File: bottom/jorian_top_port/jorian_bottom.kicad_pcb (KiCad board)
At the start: 2 copper layers, 152.4 x 85.1 mm, 7 parts

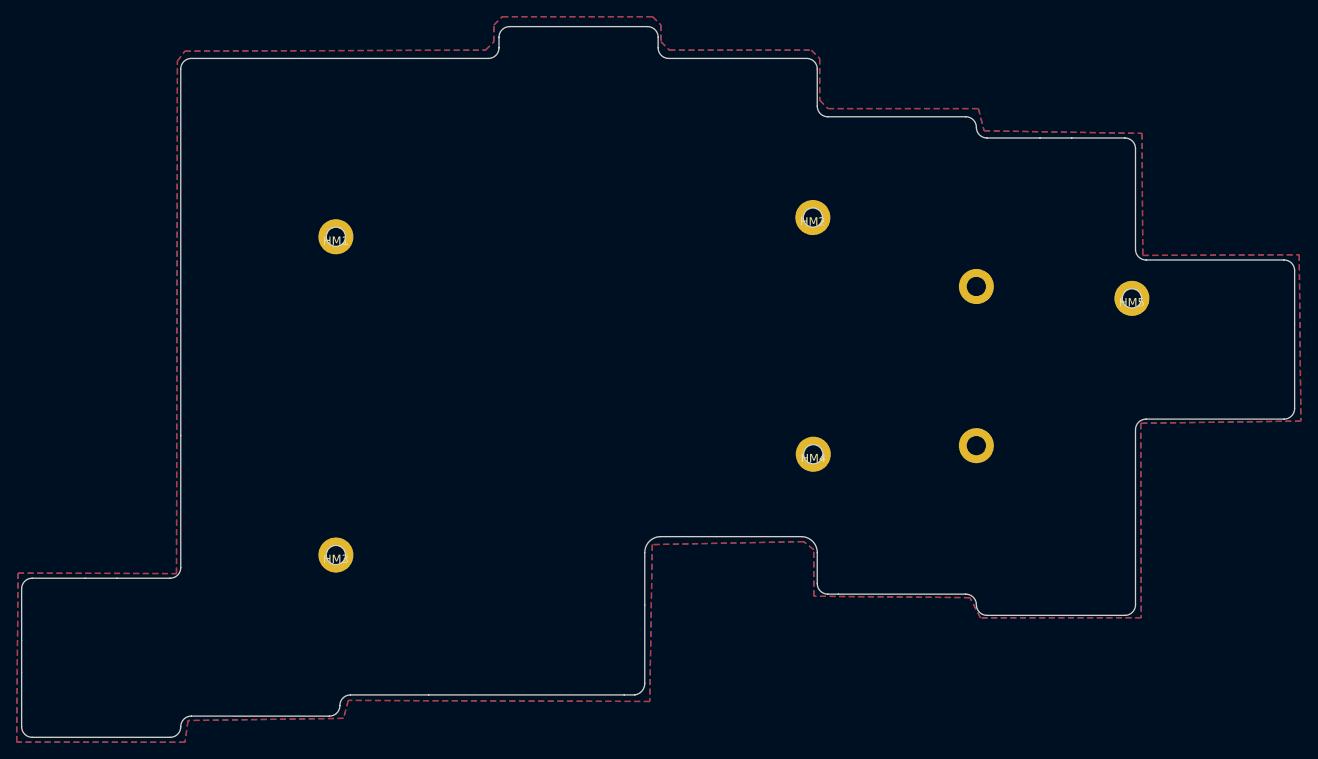
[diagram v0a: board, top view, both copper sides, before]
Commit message: Work on bottom with AA holder
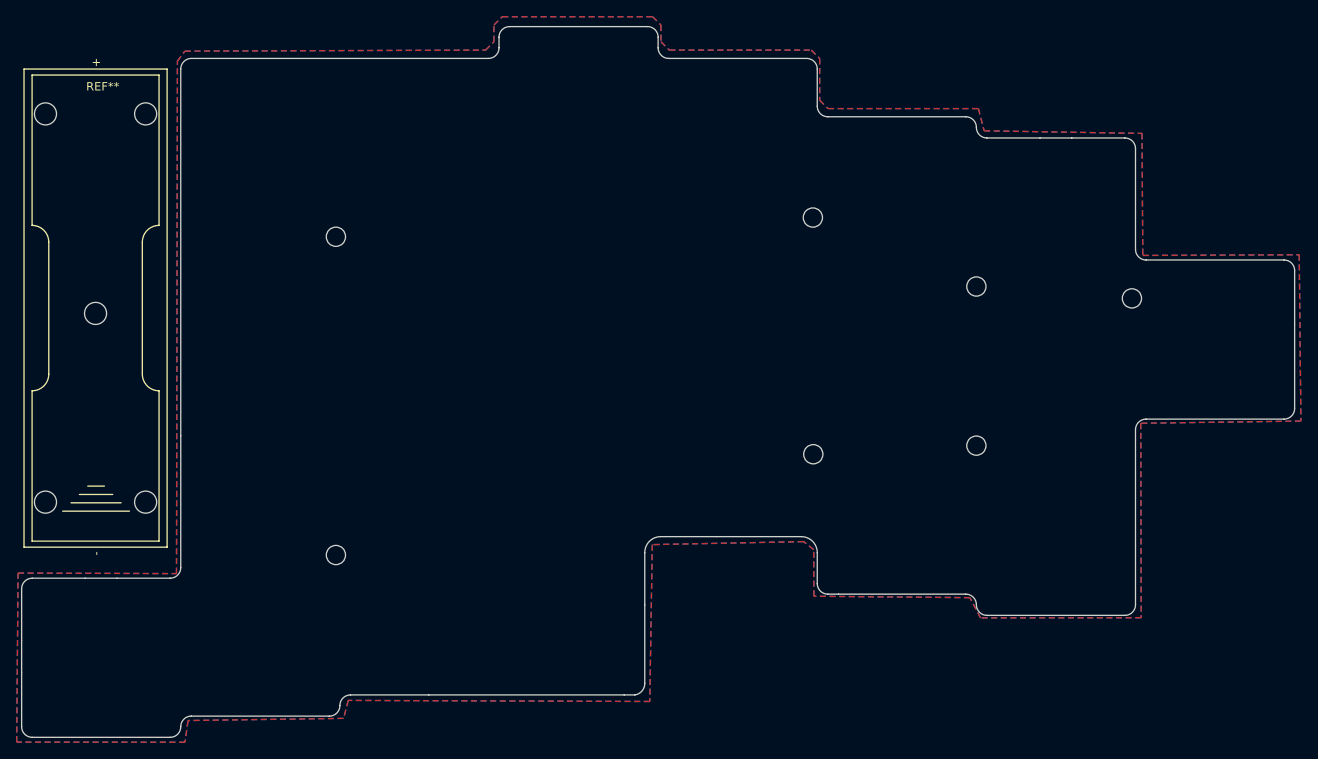
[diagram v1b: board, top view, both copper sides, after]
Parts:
- added REF**: BatteryHolder_AA, jorian:BatteryHolder_AA, F.Cu at (31.1, 73.1)
- HM1, HM2, HM3, HM4, HM5: footprint kbd:M2_Hole_TH_mod -> kbd:M2_Hole_Edge_Cut
- HM6, HM7: renamed from ?; value (none) -> CaseHole; footprint (none) -> kbd:M2_Hole_Edge_Cut
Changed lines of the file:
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@@
   (net 0 "")
   (net 1 "GND")
-  (footprint "" (layer "F.Cu")
+  (footprint "kbd:M2_Hole_Edge_Cut" (layer "F.Cu")
     (at 136.525 88.9)
-    (fp_text reference "" (at 0 0) (layer "F.SilkS")
-      (effects (font (size 1.27 1.27) (thickness 0.15)))
+    (fp_text reference "HM7" (at 0 1.9) (layer "Dwgs.User")
+      (effects (font (size 1 1) (thickness 0.15)))
     )
-    (fp_text value "" (at 0 0) (layer "F.SilkS")
-      (effects (font (size 1.27 1.27) (thickness 0.15)))
+    (fp_text value "CaseHole" (at 0 -1.8) (layer "F.Fab")
+      (effects (font (size 1 1) (thickness 0.15)))
     )
-    (pad "" thru_hole circle (at 0 0) (size 4.2 4.2) (drill 2.3) (layers *.Cu *.Mask))
+    (fp_circle (center 0 0) (end 1.15 0) (layer "Edge.Cuts") (width 0.1) (fill none))
   )
-  (footprint "kbd:M2_Hole_TH_mod" (layer "F.Cu")
+  (footprint "kbd:M2_Hole_Edge_Cut" (layer "F.Cu")
     (at 59.85 101.995)
     (property "Sheetfile" "jorian.kicad_sch")
     (property "Sheetname" "")
-    (fp_text reference "HM3" (at 0 0.5) (layer "F.SilkS")
+    (fp_text reference "HM3" (at 0 1.9) (layer "Dwgs.User")
       (effects (font (size 1 1) (thickness 0.15)))
     )
-    (fp_text value "CaseHole" (at 0 -0.5) (layer "F.Fab")
-      (effects (font (size 1 1) (thickness 0.15)))
-    )
-    (fp_text user "${REFERENCE}" (at 0.3 0) (layer "F.Fab")
+    (fp_text value "CaseHole" (at 0 -1.8) (layer "F.Fab")
       (effects (font (size 1 1) (thickness 0.15)))
     )
     (fp_circle (center 0 0) (end 1.15 0) (layer "Edge.Cuts") (width 0.1) (fill none))
-    (pad "" thru_hole circle (at 0 0) (size 4.2 4.2) (drill 2.3) (layers *.Cu *.Mask))
   )
-  (footprint "kbd:M2_Hole_TH_mod" (layer "F.Cu")
+  (footprint "jorian:BatteryHolder_AA" (layer "F.Cu")
+    (at 31.075 73.07)
+    (descr "https://www.keyelco.com/product-pdf.cfm?p=1025")
+    (tags "AA battery cell holder")
+    (attr through_hole)
+    (fp_text reference "REF**" (at 0.86 -27.15 180) (layer "F.SilkS")
+      (effects (font (size 1 1) (thickness 0.15)))
+    )
+    (fp_text value "BatteryHolder_AA" (at 0 -2.135 90) (layer "F.Fab")
+      (effects (font (size 1 1) (thickness 0.15)))
+    )
+    (fp_text user "+" (at 0.06 -30.035 270) (layer "F.SilkS")
+      (effects (font (size 1 1) (thickness 0.15)))
+    )
+    (fp_text user "-" (at 0.06 28.735 270) (layer "F.SilkS")
+      (effects (font (size 1 1) (thickness 0.15)))
+    )
+    (fp_line (start -7.6 -28.535) (end -7.6 -10.535) (layer "F.SilkS") (width 0.12))
+    (fp_line (start -7.6 9.265) (end -7.6 27.265) (layer "F.SilkS") (width 0.12))
+    (fp_line (start -8.565 -29.255) (end 8.565 -29.255) (layer "F.SilkS") (width 0.12))
+    (fp_line (start 7.6 9.265) (end 7.6 27.265) (layer "F.SilkS") (width 0.12))
+    (fp_line (start -8.565 27.985) (end -8.565 -29.255) (layer "F.SilkS") (width 0.12))
+    (fp_line (start 7.6 27.265) (end -7.6 27.265) (layer "F.SilkS") (width 0.12))
+    (fp_line (start 8.565 27.985) (end -8.565 27.985) (layer "F.SilkS") (width 0.12))
+    (fp_line (start 7.6 -28.535) (end 7.6 -10.535) (layer "F.SilkS") (width 0.12))
+    (fp_line (start -2.94 22.675) (end 3.06 22.675) (layer "F.SilkS") (width 0.12))
+    (fp_line (start 7.6 -28.535) (end -7.6 -28.535) (layer "F.SilkS") (width 0.12))
+    (fp_line (start 1.06 20.675) (end -0.94 20.675) (layer "F.SilkS") (width 0.12))
+    (fp_line (start 4.06 23.675) (end -3.94 23.675) (layer "F.SilkS") (width 0.12))
+    (fp_line (start 5.6 -8.535) (end 5.6 7.265) (layer "F.SilkS") (width 0.12))
+    (fp_line (start 8.565 -29.255) (end 8.565 27.985) (layer "F.SilkS") (width 0.12))
+    (fp_line (start -5.6 7.265) (end -5.6 -8.535) (layer "F.SilkS") (width 0.12))
+    (fp_line (start 2.06 21.675) (end -1.94 21.675) (layer "F.SilkS") (width 0.12))
+    (fp_arc (start 7.6 9.265) (mid 6.185786 8.679214) (end 5.6 7.265) (layer "F.SilkS") (width 0.12))
+    (fp_arc (start -5.6 7.265) (mid -6.185786 8.679214) (end -7.6 9.265) (layer "F.SilkS") (width 0.12))
+    (fp_arc (start 5.6 -8.535) (mid 6.185786 -9.949214) (end 7.6 -10.535) (layer "F.SilkS") (width 0.12))
+    (fp_arc (start -7.6 -10.535) (mid -6.185786 -9.949214) (end -5.6 -8.535) (layer "F.SilkS") (width 0.12))
+    (fp_line (start -8.7 28.115) (end -8.7 -29.385) (layer "F.CrtYd") (width 0.05))
+    (fp_line (start 8.7 -29.385) (end 8.7 28.115) (layer "F.CrtYd") (width 0.05))
+    (fp_line (start 8.7 28.115) (end -8.7 28.115) (layer "F.CrtYd") (width 0.05))
+    (fp_line (start -8.7 -29.385) (end 8.7 -29.385) (layer "F.CrtYd") (width 0.05))
+    (fp_line (start -8.445 -29.135) (end -8.445 27.865) (layer "F.Fab") (width 0.1))
+    (fp_line (start -8.445 27.865) (end 8.445 27.865) (layer "F.Fab") (width 0.1))
+    (fp_line (start 8.445 27.865) (end 8.445 -29.135) (layer "F.Fab") (width 0.1))
+    (fp_line (start 8.445 -29.135) (end -8.445 -29.135) (layer "F.Fab") (width 0.1))
+    (pad "" np_thru_hole circle (at 5.995 -23.885) (size 2.64 2.64) (drill 2.64) (layers *.Cu *.Mask))
+    (pad "" np_thru_hole circle (at -5.995 -23.885) (size 2.64 2.64) (drill 2.64) (layers *.Cu *.Mask))
+    (pad "" np_thru_hole circle (at -5.995 22.595 90) (size 2.64 2.64) (drill 2.64) (layers *.Cu *.Mask))
+    (pad "" np_thru_hole circle (at 0 0 270) (size 2.64 2.64) (drill 2.64) (layers *.Cu *.Mask))
+    (pad "" np_thru_hole circle (at 5.995 22.595 270) (size 2.64 2.64) (drill 2.64) (layers *.Cu *.Mask))
+    (model "${KICAD6_3DMODEL_DIR}/Battery.3dshapes/BatteryHolder_Keystone_2460_1xAA.wrl"
+      (offset (xyz 0 0 0))
+      (scale (xyz 1 1 1))
+      (rotate (xyz 0 0 0))
+    )
+  )
+  (footprint "kbd:M2_Hole_Edge_Cut" (layer "F.Cu")
     (at 155.145948 71.270959)
     (property "Sheetfile" "jorian.kicad_sch")
     (property "Sheetname" "")
-    (fp_text reference "HM5" (at 0 0.5) (layer "F.SilkS")
+    (fp_text reference "HM5" (at 0 1.9) (layer "Dwgs.User")
       (effects (font (size 1 1) (thickness 0.15)))
     )
-    (fp_text value "CaseHole" (at 0 -0.5) (layer "F.Fab")
-      (effects (font (size 1 1) (thickness 0.15)))
-    )
-    (fp_text user "${REFERENCE}" (at 0.3 0) (layer "F.Fab")
+    (fp_text value "CaseHole" (at 0 -1.8) (layer "F.Fab")
       (effects (font (size 1 1) (thickness 0.15)))
     )
     (fp_circle (center 0 0) (end 1.15 0) (layer "Edge.Cuts") (width 0.1) (fill none))
-    (pad "" thru_hole circle (at 0 0) (size 4.2 4.2) (drill 2.3) (layers *.Cu *.Mask))
   )
-  (footprint "kbd:M2_Hole_TH_mod" (layer "F.Cu")
+  (footprint "kbd:M2_Hole_Edge_Cut" (layer "F.Cu")
     (at 116.95 61.595)
     (property "Sheetfile" "jorian.kicad_sch")
     (property "Sheetname" "")
-    (fp_text reference "HM2" (at 0 0.5) (layer "F.SilkS")
+    (fp_text reference "HM2" (at 0 1.9) (layer "Dwgs.User")
       (effects (font (size 1 1) (thickness 0.15)))
     )
-    (fp_text value "CaseHole" (at 0 -0.5) (layer "F.Fab")
-      (effects (font (size 1 1) (thickness 0.15)))
-    )
-    (fp_text user "${REFERENCE}" (at 0.3 0) (layer "F.Fab")
+    (fp_text value "CaseHole" (at 0 -1.8) (layer "F.Fab")
       (effects (font (size 1 1) (thickness 0.15)))
     )
     (fp_circle (center 0 0) (end 1.15 0) (layer "Edge.Cuts") (width 0.1) (fill none))
-    (pad "" thru_hole circle (at 0 0) (size 4.2 4.2) (drill 2.3) (layers *.Cu *.Mask))
   )
-  (footprint "" (layer "F.Cu")
+  (footprint "kbd:M2_Hole_Edge_Cut" (layer "F.Cu")
     (at 136.525 69.85)
-    (fp_text reference "" (at 0 0) (layer "F.SilkS")
-      (effects (font (size 1.27 1.27) (thickness 0.15)))
+    (fp_text reference "HM6" (at 0 1.9) (layer "Dwgs.User")
+      (effects (font (size 1 1) (thickness 0.15)))
     )
-    (fp_text value "" (at 0 0) (layer "F.SilkS")
-      (effects (font (size 1.27 1.27) (thickness 0.15)))
+    (fp_text value "CaseHole" (at 0 -1.8) (layer "F.Fab")
+      (effects (font (size 1 1) (thickness 0.15)))
     )
-    (pad "" thru_hole circle (at 0 0) (size 4.2 4.2) (drill 2.3) (layers *.Cu *.Mask))
+    (fp_circle (center 0 0) (end 1.15 0) (layer "Edge.Cuts") (width 0.1) (fill none))
   )
-  (footprint "kbd:M2_Hole_TH_mod" (layer "F.Cu")
+  (footprint "kbd:M2_Hole_Edge_Cut" (layer "F.Cu")
     (at 117 89.93)
     (property "Sheetfile" "jorian.kicad_sch")
     (property "Sheetname" "")
-    (fp_text reference "HM4" (at 0 0.5) (layer "F.SilkS")
+    (fp_text reference "HM4" (at 0 1.9) (layer "Dwgs.User")
       (effects (font (size 1 1) (thickness 0.15)))
     )
-    (fp_text value "CaseHole" (at 0 -0.5) (layer "F.Fab")
-      (effects (font (size 1 1) (thickness 0.15)))
-    )
-    (fp_text user "${REFERENCE}" (at 0.3 0) (layer "F.Fab")
+    (fp_text value "CaseHole" (at 0 -1.8) (layer "F.Fab")
       (effects (font (size 1 1) (thickness 0.15)))
     )
     (fp_circle (center 0 0) (end 1.15 0) (layer "Edge.Cuts") (width 0.1) (fill none))
-    (pad "" thru_hole circle (at 0 0) (size 4.2 4.2) (drill 2.3) (layers *.Cu *.Mask))
   )
-  (footprint "kbd:M2_Hole_TH_mod" (layer "F.Cu")
+  (footprint "kbd:M2_Hole_Edge_Cut" (layer "F.Cu")
     (at 59.85 63.895)
     (property "Sheetfile" "jorian.kicad_sch")
     (property "Sheetname" "")
-    (fp_text reference "HM1" (at 0 0.5) (layer "F.SilkS")
+    (fp_text reference "HM1" (at 0 1.9) (layer "Dwgs.User")
       (effects (font (size 1 1) (thickness 0.15)))
     )
-    (fp_text value "CaseHole" (at 0 -0.5) (layer "F.Fab")
-      (effects (font (size 1 1) (thickness 0.15)))
-    )
-    (fp_text user "${REFERENCE}" (at 0.3 0) (layer "F.Fab")
+    (fp_text value "CaseHole" (at 0 -1.8) (layer "F.Fab")
       (effects (font (size 1 1) (thickness 0.15)))
     )
     (fp_circle (center 0 0) (end 1.15 0) (layer "Edge.Cuts") (width 0.1) (fill none))
-    (pad "" thru_hole circle (at 0 0) (size 4.2 4.2) (drill 2.3) (layers *.Cu *.Mask))
   )
   (gr_arc (start 97.155 38.735) (mid 98.053026 39.106974) (end 98.425 40.005) (layer "Edge.Cuts") (width 0.15))
